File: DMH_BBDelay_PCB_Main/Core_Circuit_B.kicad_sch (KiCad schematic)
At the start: 73 parts, among them Q8 J113, SW1 SW_SPDT, SW2 SW_DPDT_x2, SW4 SW_SPDT, U18 CD4053B, U5 TL074, U6 TL074, U7 V3205, U8 CD4046, U9 40106

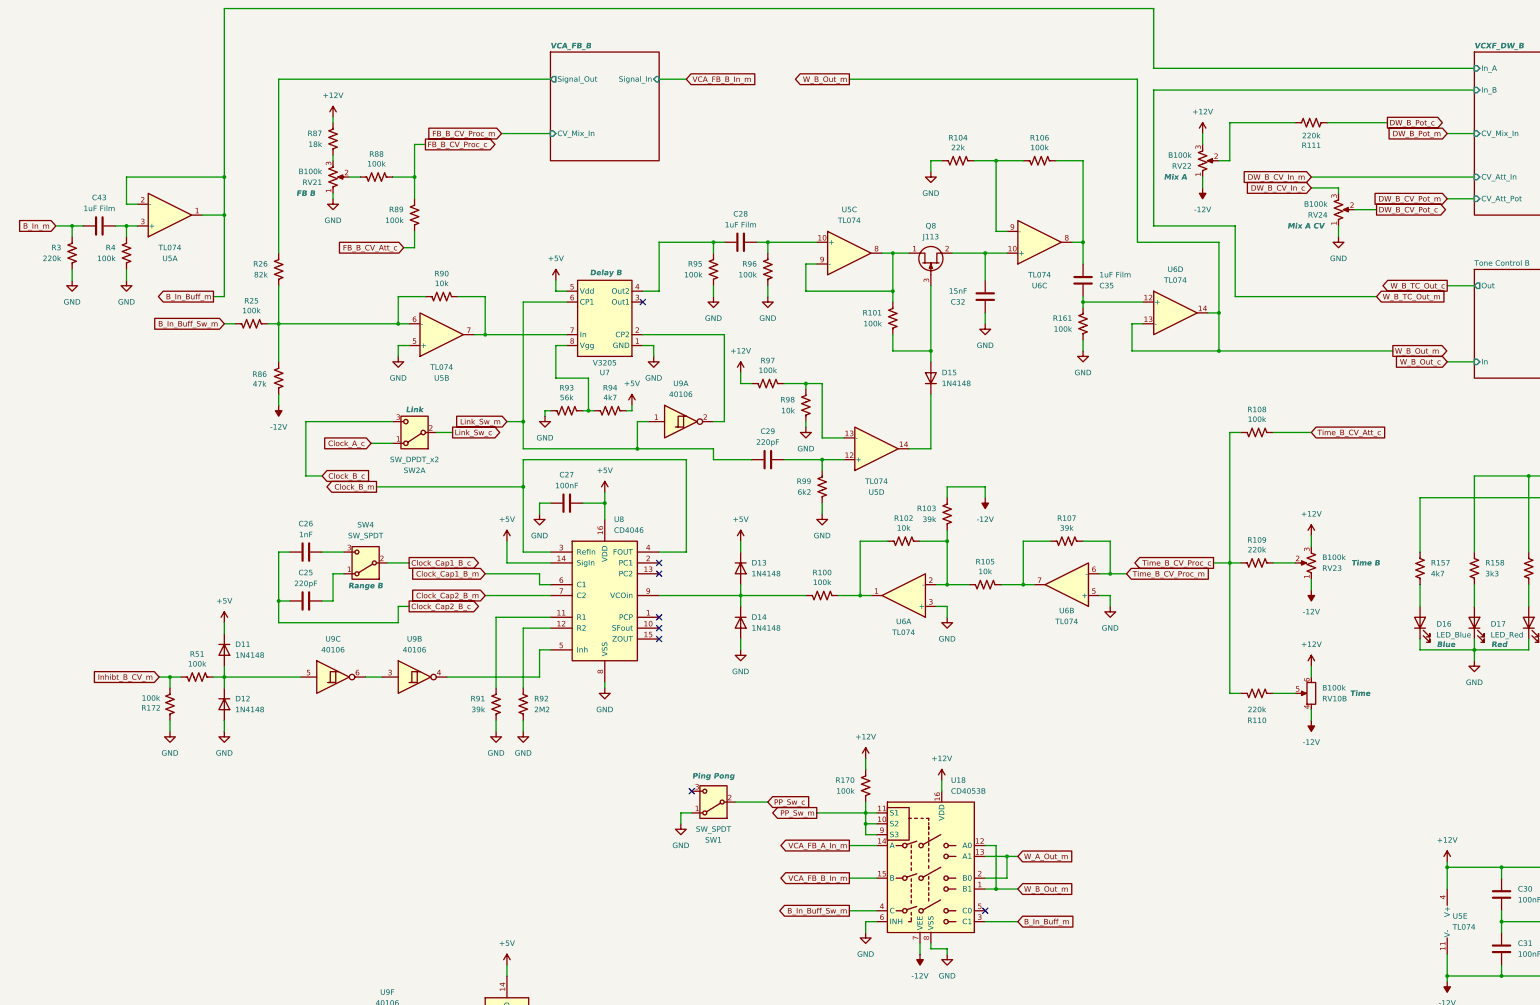
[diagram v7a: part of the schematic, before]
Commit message: Switch to route Dry A to B VCXF input in PP mode
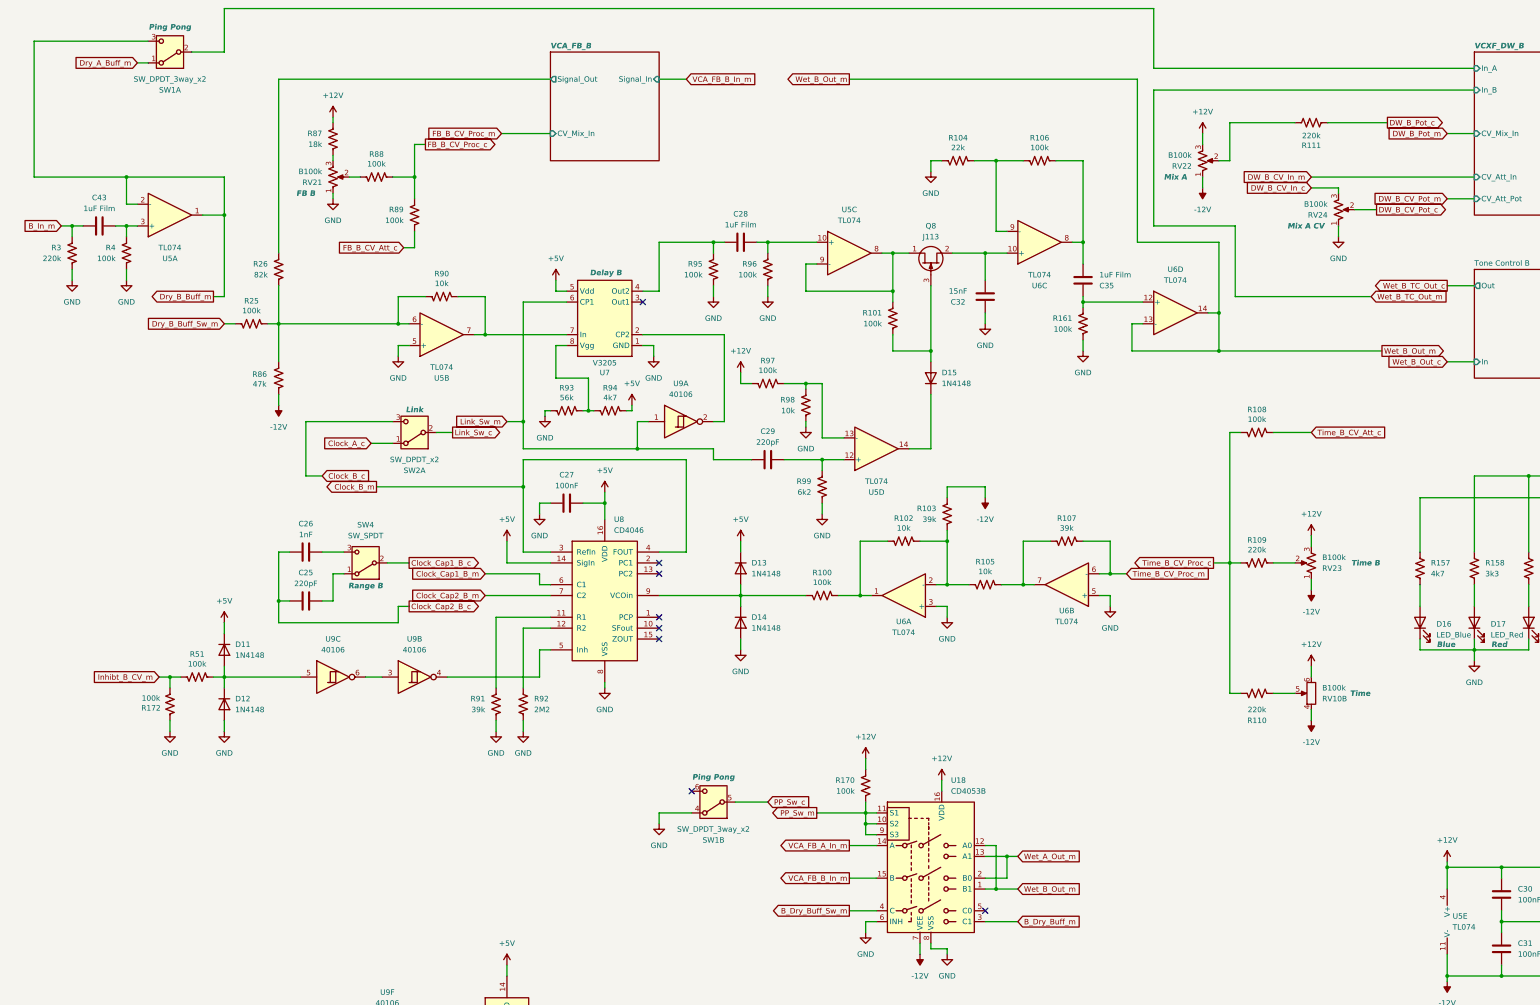
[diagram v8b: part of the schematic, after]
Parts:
- removed SW1: SW_SPDT, symbol Switch:SW_SPDT
- added SW1: SW_DPDT_3way_x2, symbol Switch:SW_DPDT_x2
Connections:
- net GND: now also SW1.4 (A)
- net PP_Sw_c: now also SW1.5 (B)
- net B_In_Buff_Sw_m renamed B_Dry_Buff_Sw_m
- net B_Dry_Buff_Sw_m: no longer R25.1
- net B_In_Buff_m renamed Dry_B_Buff_m
- net Dry_B_Buff_m: now also SW1.3 (C); no longer U18.3 (C1)
- net W_A_Out_m renamed Wet_A_Out_m
- net W_B_Out_m renamed Wet_B_Out_m
- new net B_Dry_Buff_m: U18.3 (C1)
- new net Dry_A_Buff_m: SW1.1 (A)
- new net Dry_B_Buff_Sw_m: R25.1
- new net VCXF_DW_B/In_A: SW1.2 (B)
